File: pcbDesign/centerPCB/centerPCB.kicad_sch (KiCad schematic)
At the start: 4 parts, among them J1 Conn_01x07_Pin, J2 Conn_01x12_Pin

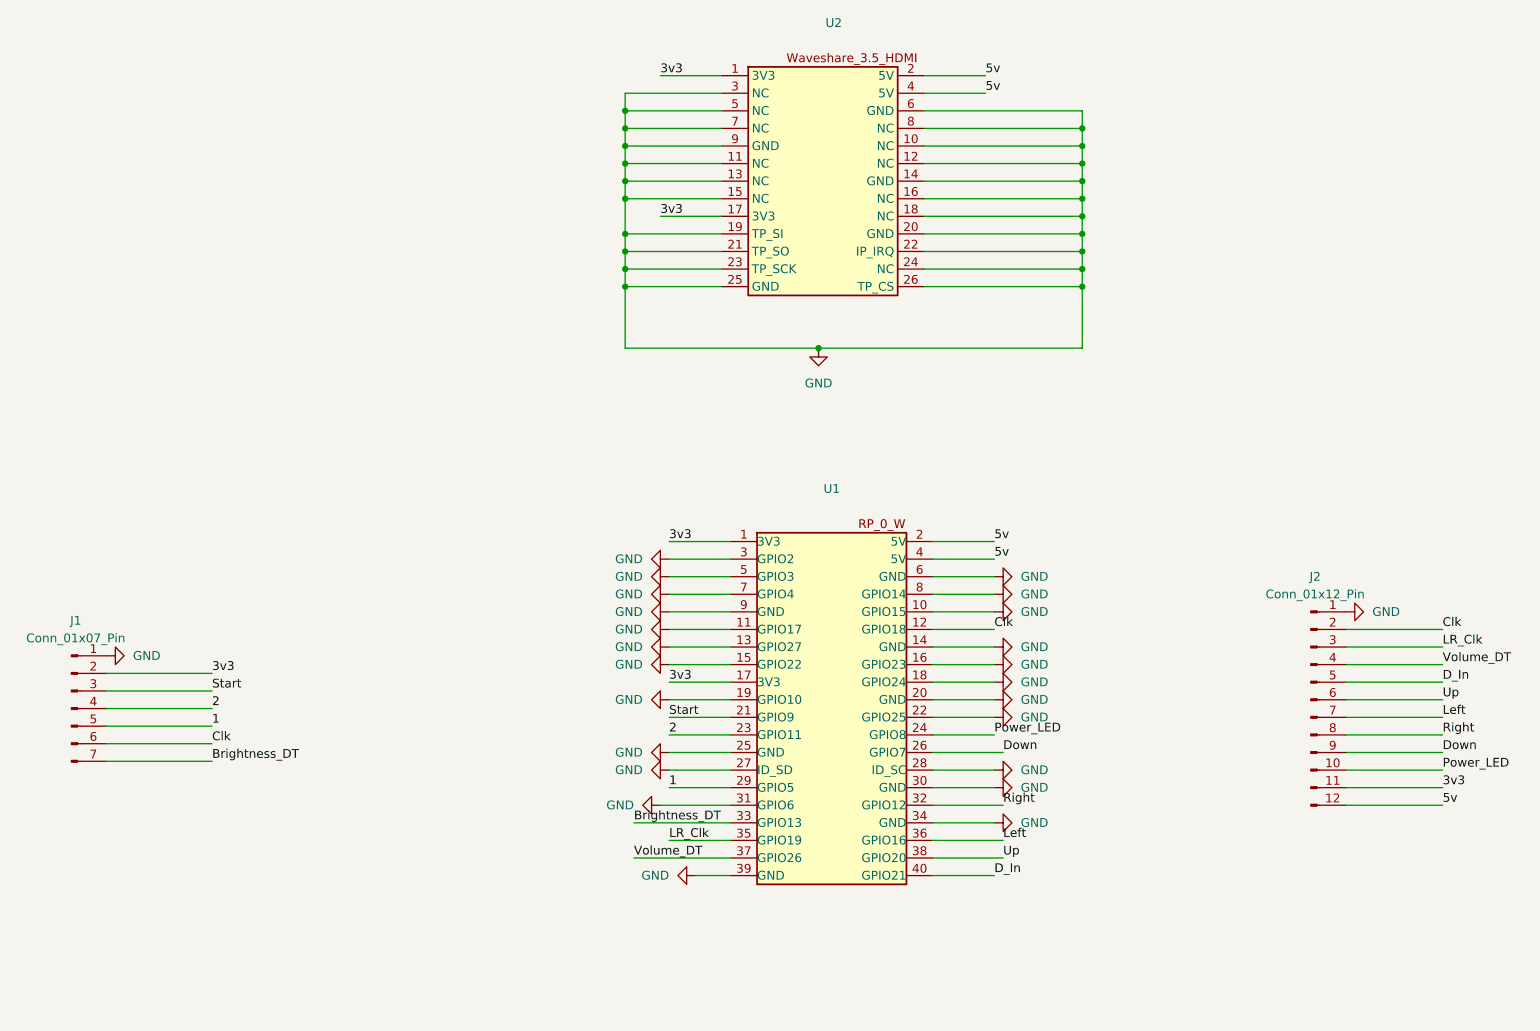
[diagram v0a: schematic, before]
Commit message: Updated pcbs and added footprint for rotary encoder (in progress)
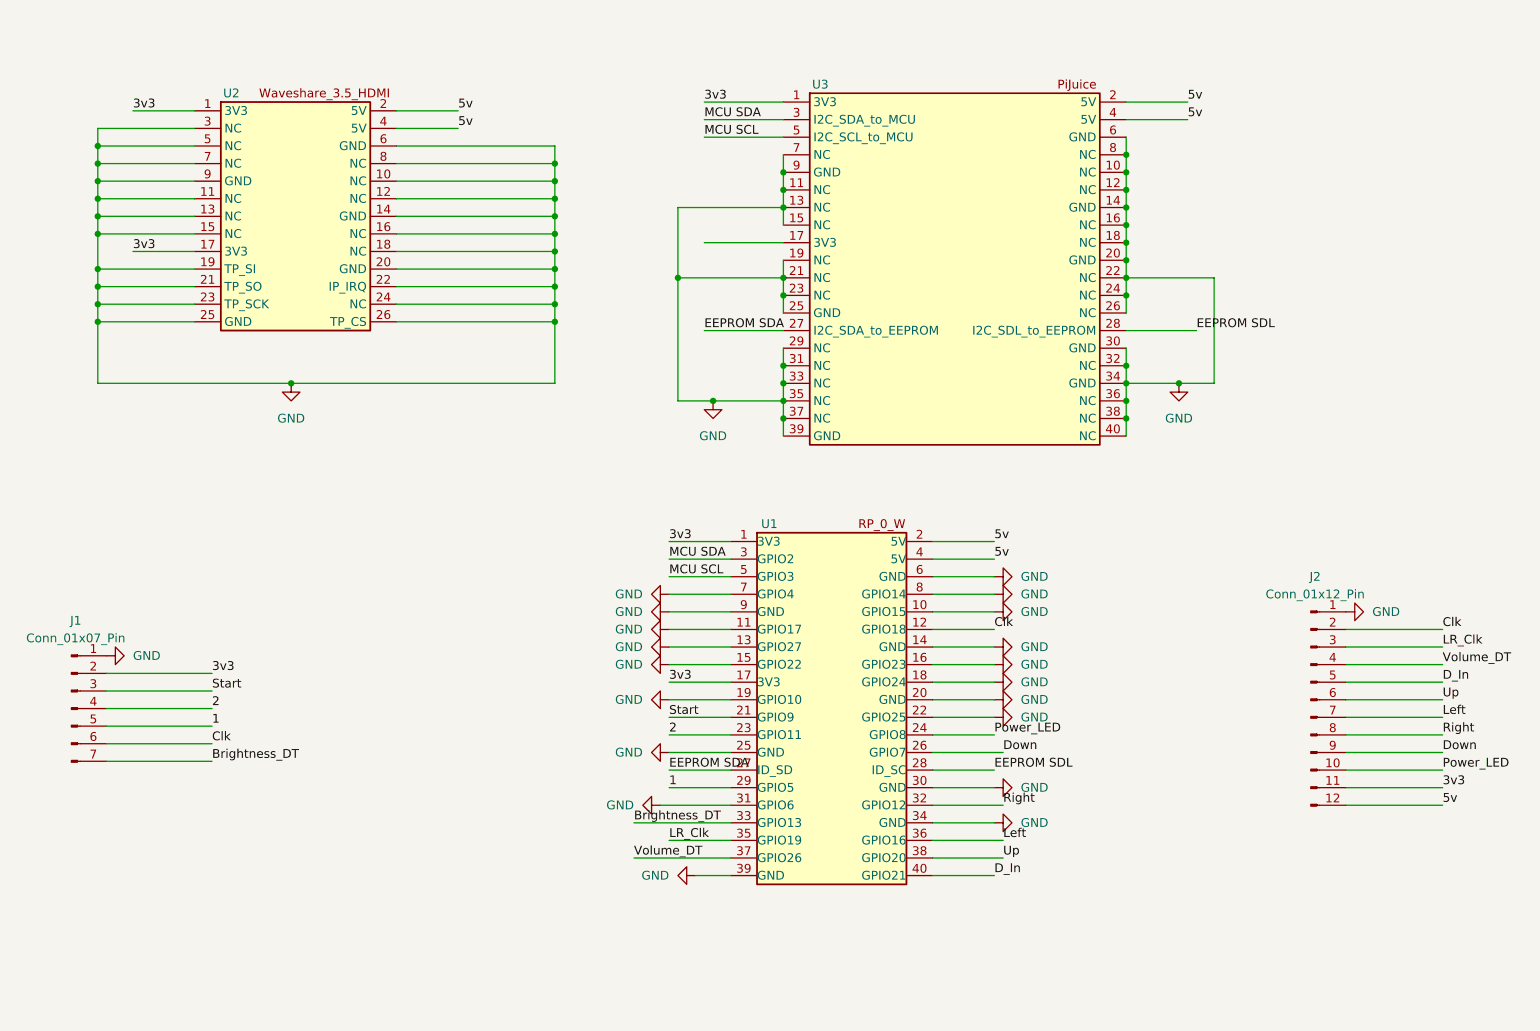
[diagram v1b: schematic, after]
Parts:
- added U3: ~, Connector_PinHeader_2.54mm:PinHeader_2x20_P2.54mm_Vertical, symbol GGMainPCB:PiJuice
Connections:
- net 3v3: now also U3.1 (3V3)
- net 5v: now also U3.2 (5V), U3.4 (5V)
- net GND: now also U3.10 (NC), U3.11 (NC), U3.12 (NC), U3.13 (NC), U3.14 (GND), U3.15 (NC), U3.16 (NC), U3.18 (NC), U3.19 (NC), U3.20 (GND), U3.21 (NC), U3.22 (NC), U3.23 (NC), U3.24 (NC), U3.25 (GND), U3.26 (NC), U3.29 (NC), U3.30 (GND), U3.31 (NC), U3.32 (NC), U3.33 (NC), U3.34 (GND), U3.35 (NC), U3.36 (NC), U3.37 (NC), U3.38 (NC), U3.39 (GND), U3.40 (NC), U3.6 (GND), U3.7 (NC), U3.8 (NC), U3.9 (GND); no longer U1.27 (ID_SD), U1.28 (ID_SC), U1.3 (GPIO2), U1.5 (GPIO3)
- new net EEPROM SDA: U1.27 (ID_SD), U3.27 (I2C_SDA_to_EEPROM)
- new net EEPROM SDL: U1.28 (ID_SC), U3.28 (I2C_SDL_to_EEPROM)
- new net MCU SCL: U1.5 (GPIO3), U3.5 (I2C_SCL_to_MCU)
- new net MCU SDA: U1.3 (GPIO2), U3.3 (I2C_SDA_to_MCU)
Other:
- moved on the sheet: U2

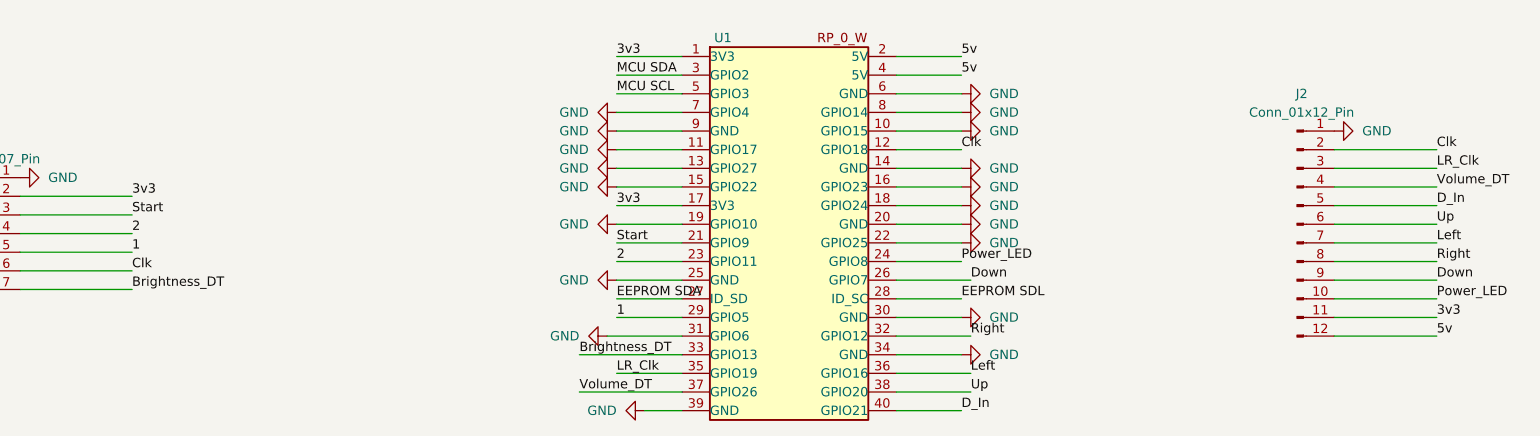
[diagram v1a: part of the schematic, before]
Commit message: finalized center pcb component placement
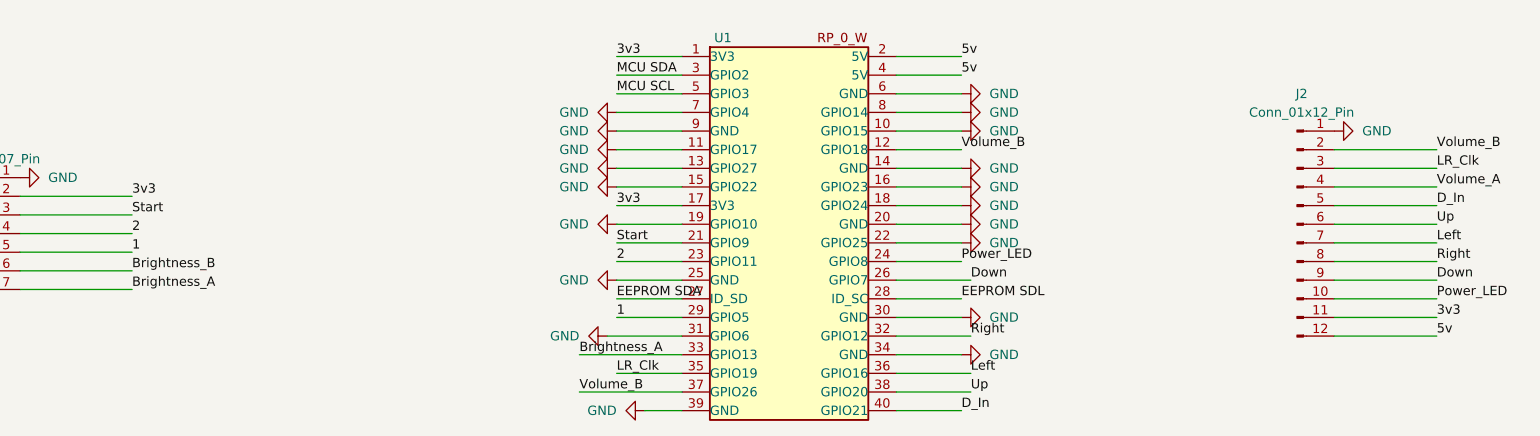
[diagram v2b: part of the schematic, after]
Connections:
- net Brightness_DT renamed Brightness_A
- net Clk renamed Volume_B
- net Volume_B: now also U1.37 (GPIO26); no longer J1.6 (Pin_6)
- net Volume_DT renamed Volume_A
- net Volume_A: no longer U1.37 (GPIO26)
- new net Brightness_B: J1.6 (Pin_6)
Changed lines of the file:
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@@
 		)
 	)
-	(label "Volume_DT"
+	(label "Volume_B"
 		(at 121.92 138.43 0)
 		(effects
@@
 		)
 	)
-	(label "Clk"
+	(label "Brightness_B"
 		(at 60.96 121.92 0)
 		(effects
@@
 		)
 	)
-	(label "Clk"
+	(label "Volume_B"
 		(at 173.99 105.41 0)
 		(effects
@@
 		)
 	)
-	(label "Clk"
+	(label "Volume_B"
 		(at 238.76 105.41 0)
 		(effects
@@
 		)
 	)
-	(label "Brightness_DT"
+	(label "Brightness_A"
 		(at 60.96 124.46 0)
 		(effects
@@
 		)
 	)
-	(label "Brightness_DT"
+	(label "Brightness_A"
 		(at 121.92 133.35 0)
 		(effects
@@
 		)
 	)
-	(label "Volume_DT"
+	(label "Volume_A"
 		(at 238.76 110.49 0)
 		(effects

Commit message: routed centerpcb
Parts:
- added H1, H2, H3: MountingHole, MountingHole:MountingHole_2.1mm, symbol Mechanical:MountingHole
- added H4, H5, H6: MountingHole, MountingHole:MountingHole_2.5mm, symbol Mechanical:MountingHole

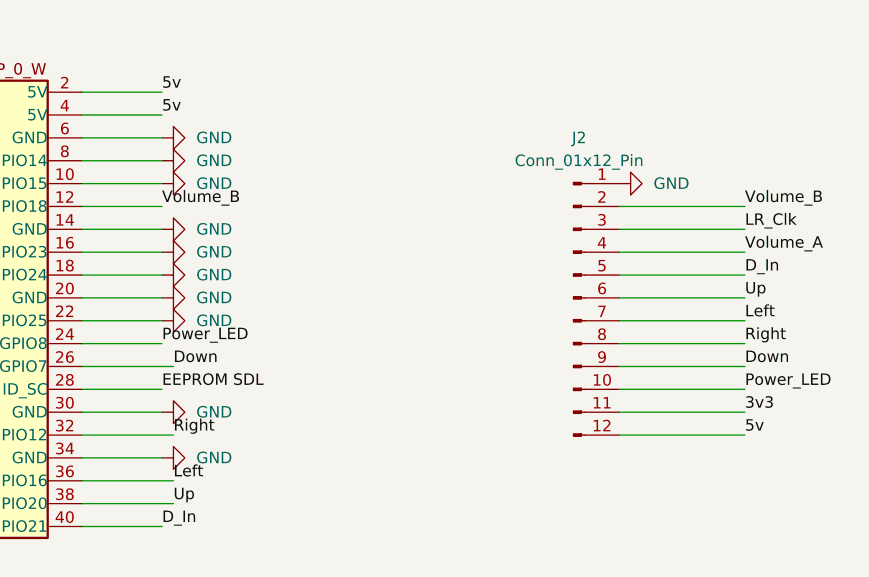
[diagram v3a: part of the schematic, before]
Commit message: Updated left header pins
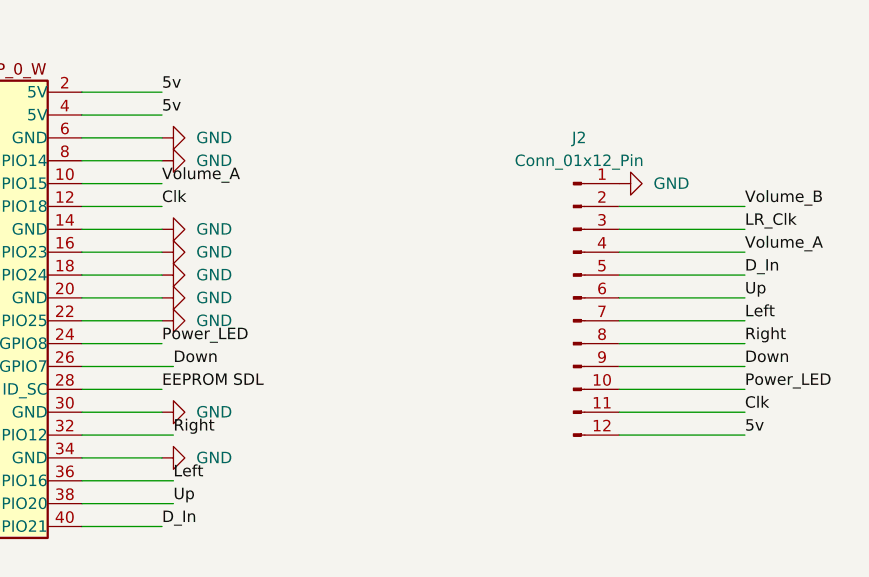
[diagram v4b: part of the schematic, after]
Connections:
- net 3v3: no longer J2.11 (Pin_11)
- net GND: no longer U1.10 (GPIO15)
- net Volume_A: now also U1.10 (GPIO15)
- net Volume_B: no longer U1.12 (GPIO18)
- new net Clk: J2.11 (Pin_11), U1.12 (GPIO18)
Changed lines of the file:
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@@
 		)
 	)
-	(label "Volume_B"
+	(label "Clk"
 		(at 173.99 105.41 0)
 		(effects
@@
 		)
 	)
+	(label "Volume_A"
+		(at 173.99 102.87 0)
+		(effects
+			(font
+				(size 1.27 1.27)
+			)
+			(justify left bottom)
+		)
+	)
 	(label "3v3"
 		(at 60.96 111.76 0)
@@
 		)
 	)
-	(label "3v3"
+	(label "Clk"
 		(at 238.76 128.27 0)
 		(effects
@@
 					(unit 1)
 				)
-			)
-		)
-	)
-	(symbol
-		(lib_id "power:GND")
-		(at 173.99 102.87 90)
-		(unit 1)
-		(exclude_from_sim no)
-		(in_bom yes)
-		(on_board yes)
-		(dnp no)
-		(fields_autoplaced yes)
-		(property "Reference" "#PWR017"
-			(at 180.34 102.87 0)
-			(effects
-				(font
-					(size 1.27 1.27)
-				)
-				(hide yes)
-			)
-		)
-		(property "Value" "GND"
-			(at 177.8 102.8699 90)
-			(effects
-				(font
-					(size 1.27 1.27)
-				)
-				(justify right)
-			)
-		)
-		(property "Footprint" ""
-			(at 173.99 102.87 0)
-			(effects
-				(font
-					(size 1.27 1.27)
-				)
-				(hide yes)
-			)
-		)
-		(property "Datasheet" ""
-			(at 173.99 102.87 0)
-			(effects
-				(font
-					(size 1.27 1.27)
-				)
-				(hide yes)
-			)
-		)
-		(property "Description" "Power symbol creates a global label with name \"GND\" , ground"
-			(at 173.99 102.87 0)
-			(effects
-				(font
-					(size 1.27 1.27)
-				)
-				(hide yes)
-			)
-		)
-		(pin "1"
-		)
-		(instances
-			(project "centerPCB"
-				(path "/4b6221a4-9608-4610-bb22-a7571fd9b838"
-					(reference "#PWR017")
-					(unit 1)
-				)

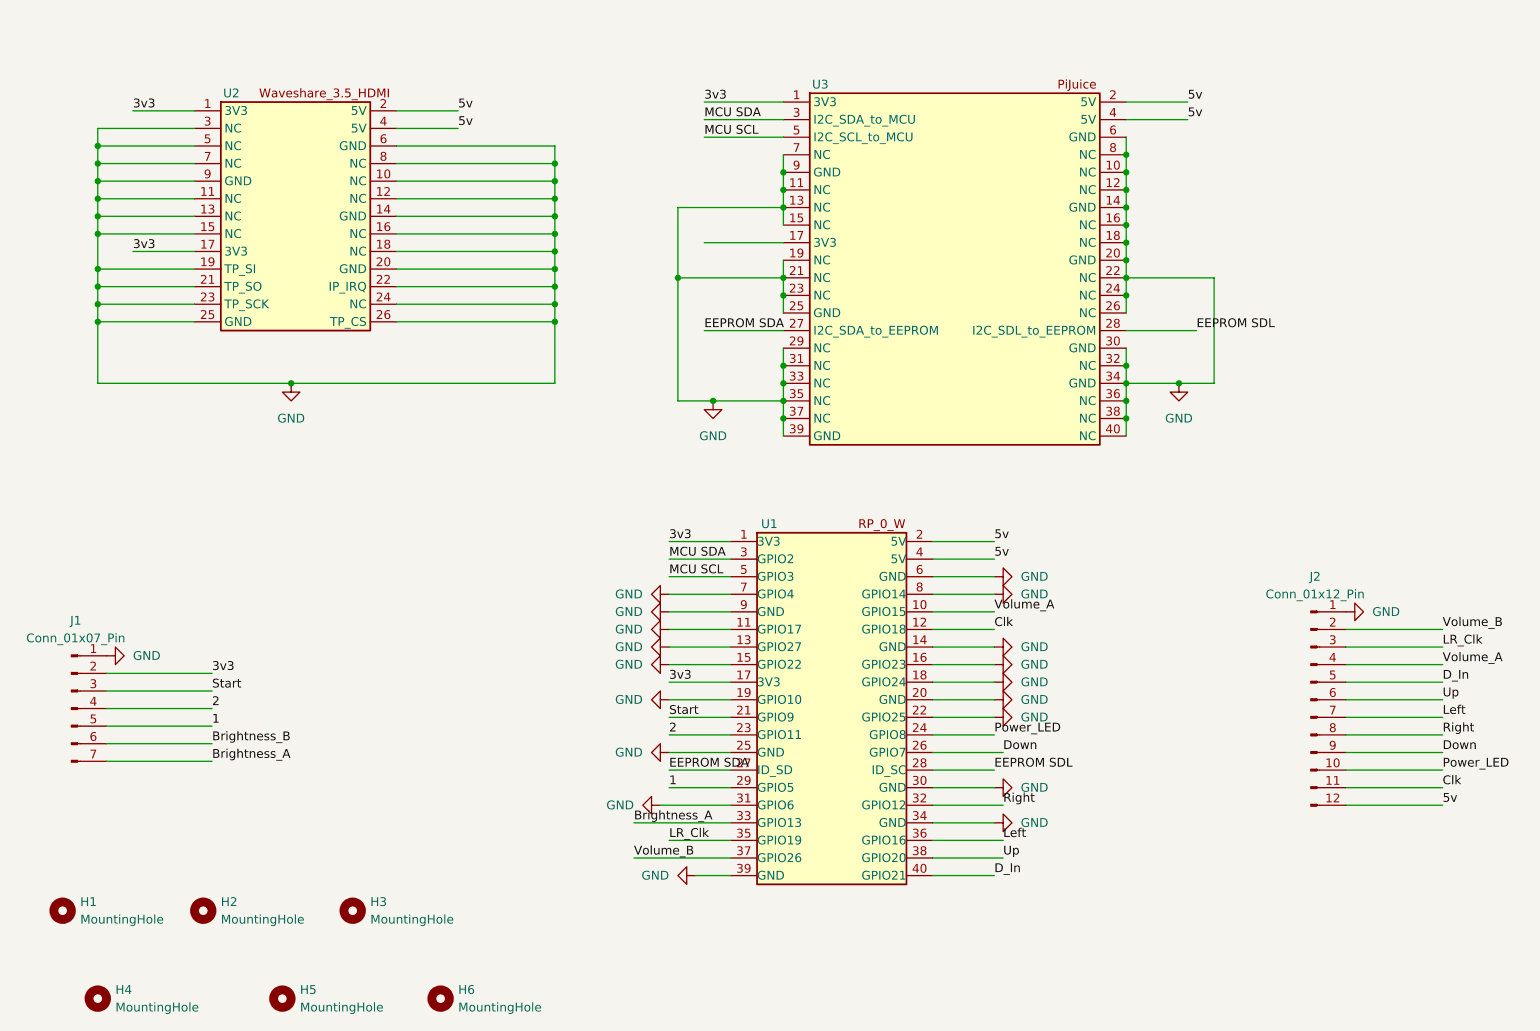
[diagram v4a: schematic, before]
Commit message: Finalized center and left pcbs placemnt
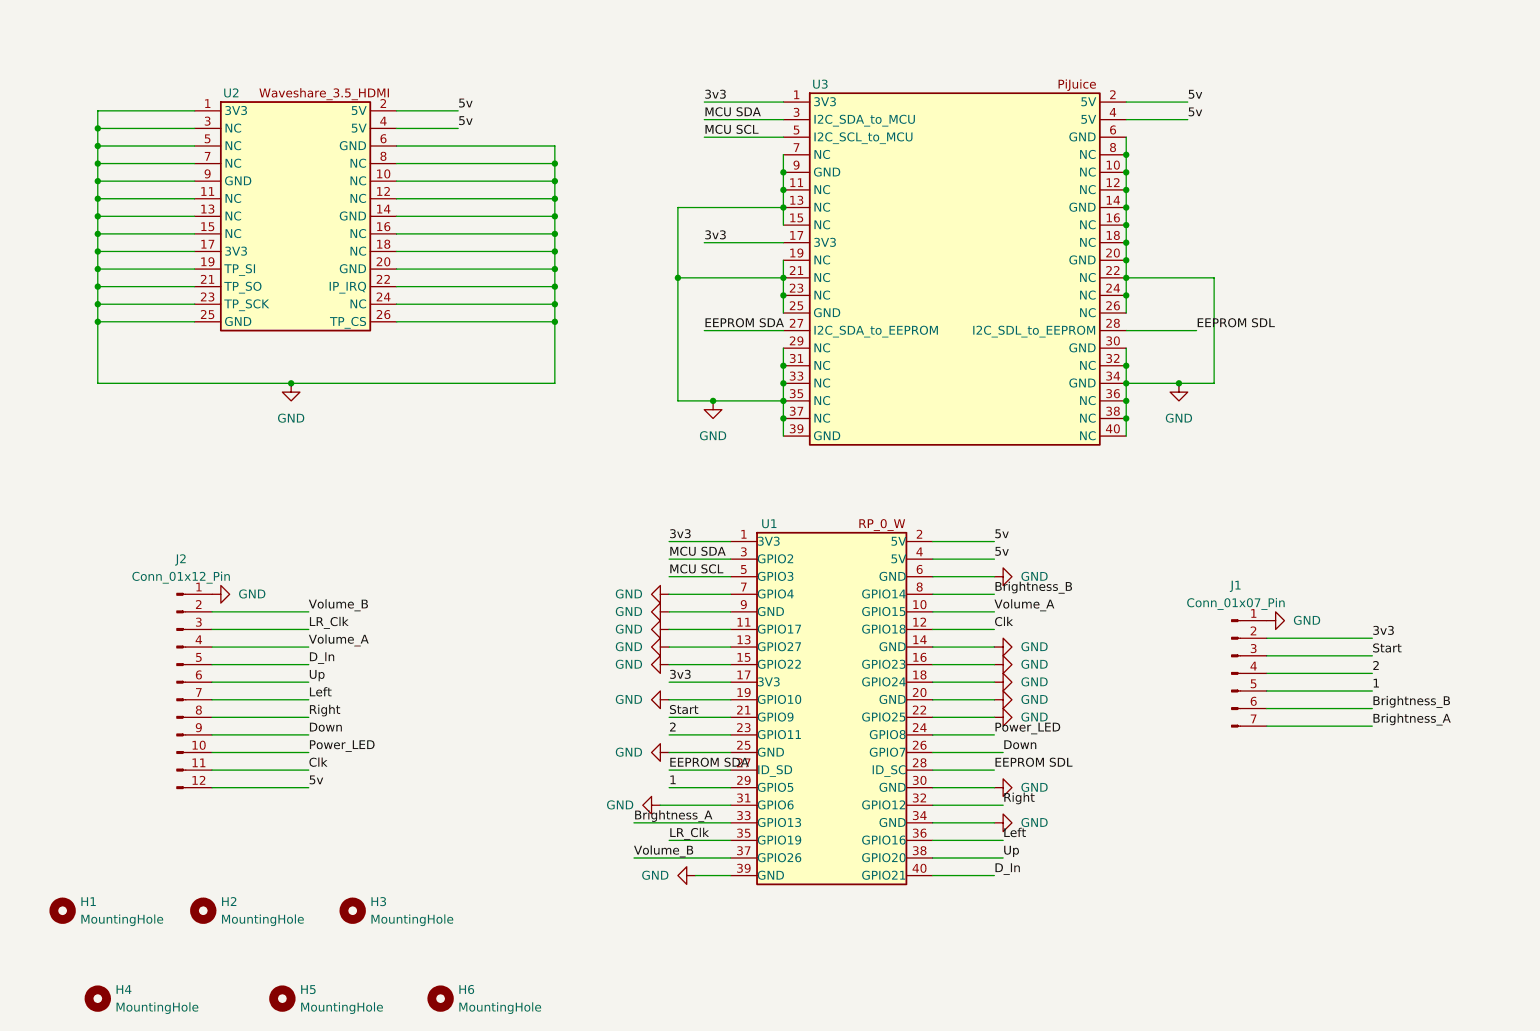
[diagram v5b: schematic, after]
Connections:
- net 3v3: now also U3.17 (3V3); no longer U2.1 (3V3), U2.17 (3V3)
- net Brightness_B: now also U1.8 (GPIO14)
- net GND: now also U2.1 (3V3), U2.17 (3V3); no longer U1.8 (GPIO14)
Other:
- moved on the sheet: J1, J2
